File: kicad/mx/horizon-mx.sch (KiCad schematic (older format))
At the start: 115 parts, among them SW1 SW_Push, SW10 SW_Push, SW11 SW_Push, SW12 SW_Push, SW13 SW_Push, SW14 SW_Push, SW15 SW_Push, SW16 SW_Push, SW17 SW_Push, SW18 SW_Push, SW19 SW_Push, SW2 SW_Push, SW20 SW_Push, SW21 SW_Push, SW22 SW_Push, SW23 SW_Push, SW24 SW_Push, SW25 SW_Push, SW26 SW_Push, SW27 SW_Push, SW28 SW_Push, SW29 SW_Push, SW3 SW_Push, SW30 SW_Push, SW31 SW_Push, SW32 SW_Push, SW33 SW_Push, SW34 SW_Push, SW35 SW_Push, SW36 SW_Push, SW37 SW_Push, SW38 SW_Push, SW39 SW_Push, SW4 SW_Push, SW40 SW_Push, SW41 SW_Push, SW42 SW_Push, SW43 SW_Push, SW44 SW_Push, SW45 SW_Push, SW46 SW_Push, SW47 SW_Push, SW48 SW_Push, SW49 SW_Push, SW5 SW_Push, SW50 SW_Push, SW51 SW_Push, SW52 SW_Push, SW6 SW_Push, SW7 SW_Push, SW8 SW_Push, SW9 SW_Push, U1 PRO-MICRO

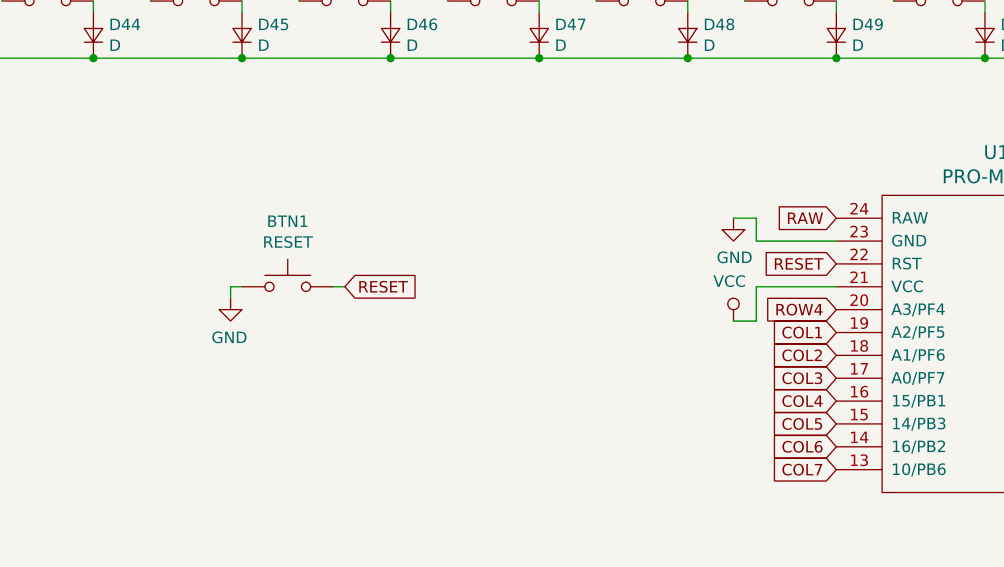
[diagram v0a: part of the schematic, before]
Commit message: Clean up plate cuts, update MX board with battery removed
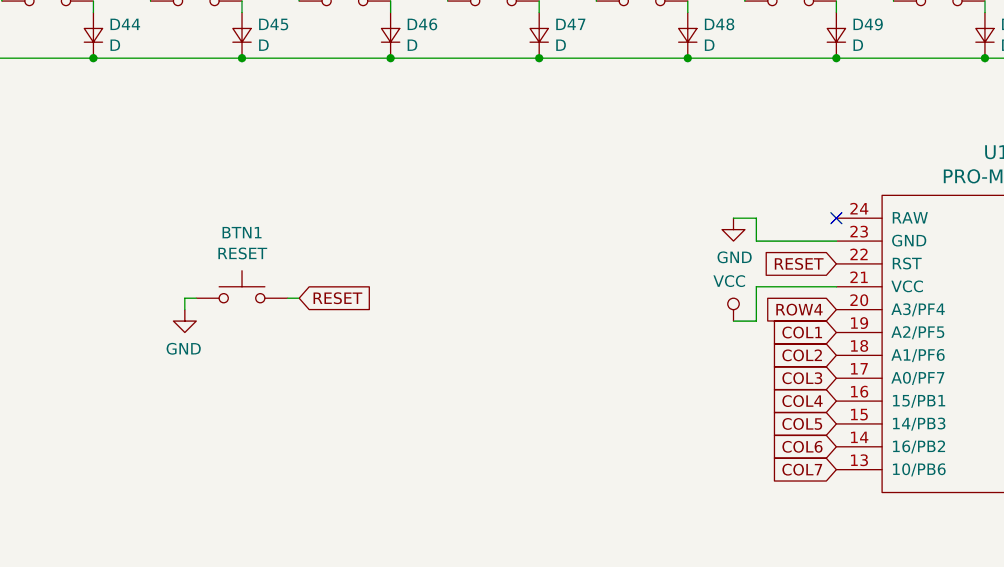
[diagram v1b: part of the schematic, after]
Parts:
- SW1, SW10, SW11, SW12, SW13, SW14, SW15, SW16, SW17, SW18, SW19, SW2, SW20, SW21, SW22, SW23, SW24, SW25, SW26, SW27, SW28, SW29, SW3, SW30, SW31, SW32, SW33, SW34, SW35, SW36, SW37, SW38, SW39, SW4, SW40, SW41, SW42, SW43, SW44, SW45, SW46, SW47, SW48, SW49, SW5, SW50, SW51, SW52, SW6, SW7, SW8, SW9: footprint horizon-footprints:SW_Choc -> horizon-footprints:SW_MX
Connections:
- net RAW: no longer names the net of U1.24 (RAW)
- no-connect marks 8 -> 9
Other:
- moved on the sheet: BTN1

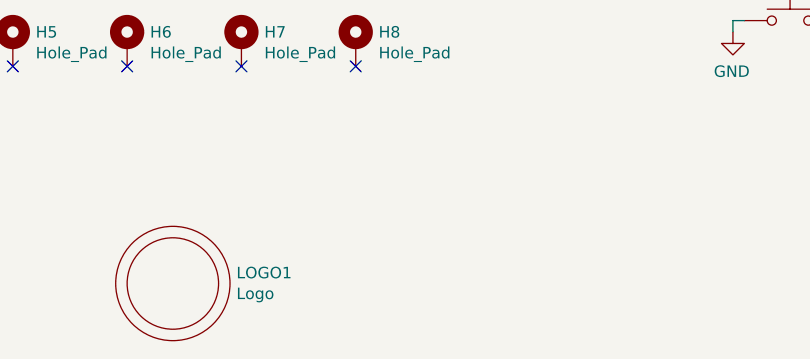
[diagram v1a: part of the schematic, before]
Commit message: Preserve logos on plate PCBs
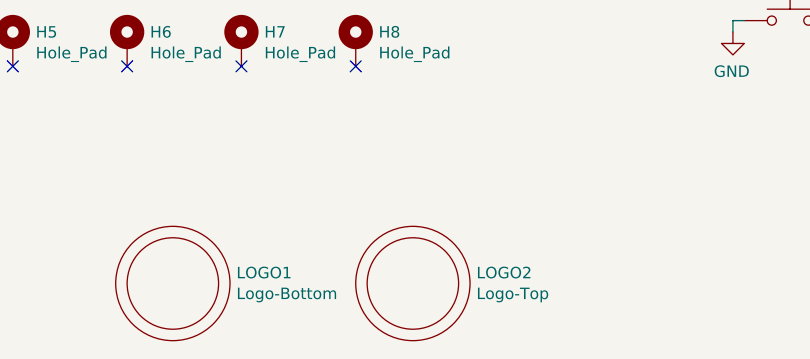
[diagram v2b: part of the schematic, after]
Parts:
- added LOGO2: Logo-Top, horizon-footprints:Logo_Horizon_H, symbol horizon-components:Logo
- LOGO1: value Logo -> Logo-Bottom
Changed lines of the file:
@@
 EESchema Schematic File Version 4
-LIBS:horizon-cache
+LIBS:horizon-mx-cache
 EELAYER 30 0
 EELAYER END
@@
 P 2400 6400
 F 0 "LOGO1" H 2678 6446 50  0000 L CNN
-F 1 "Logo" H 2678 6355 50  0000 L CNN
+F 1 "Logo-Bottom" H 2678 6355 50  0000 L CNN
 F 2 "horizon-footprints:Logo_Horizon_Small" H 2400 6350 50  0001 C CNN
 F 3 "" H 2400 6350 50  0001 C CNN
@@
 Text GLabel 5350 5250 2    50   Input ~ 0
 RESET
+$Comp
+L horizon-components:Logo LOGO2
+U 1 1 614B138E
+P 3450 6400
+F 0 "LOGO2" H 3728 6446 50  0000 L CNN
+F 1 "Logo-Top" H 3728 6355 50  0000 L CNN
+F 2 "horizon-footprints:Logo_Horizon_H" H 3450 6350 50  0001 C CNN
+F 3 "" H 3450 6350 50  0001 C CNN
+	1    3450 6400
+	1    0    0    -1
+$EndComp
 $EndSCHEMATC
